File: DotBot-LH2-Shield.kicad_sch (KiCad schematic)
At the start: 15 parts, among them J1 Conn_01x04, J1 Conn_01x10, U1 LSM303AGR, U4 TS4231

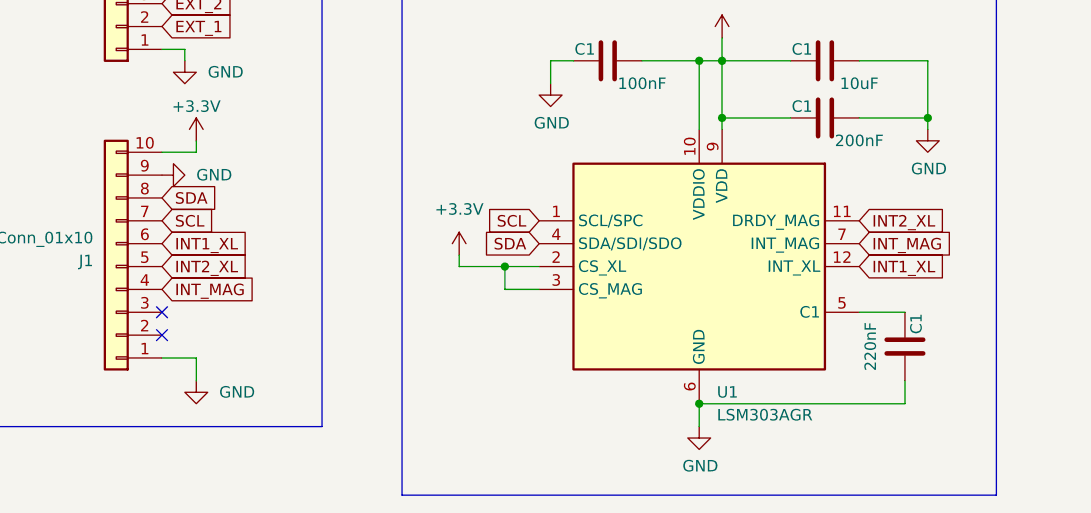
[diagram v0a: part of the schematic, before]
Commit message: Add LH2 shield BOM
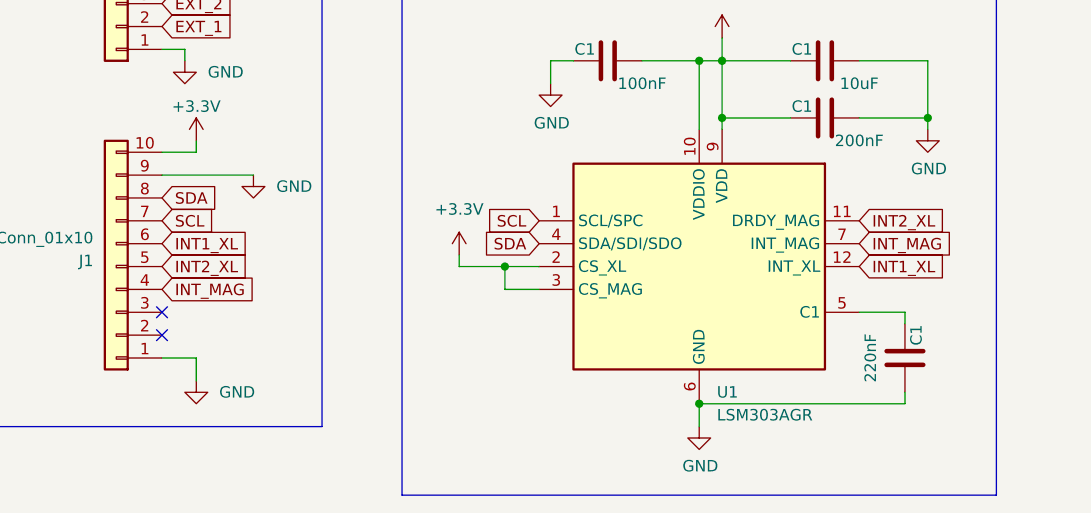
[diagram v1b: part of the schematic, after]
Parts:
- C1, C9: Price $0.005 -> 0.005
- C2: Price $0.0085 -> 0.0085
- D1: Price $0.49 -> 0.49
- D2: Price $0.146 -> 0.146
- J1: Price (none) -> 0.0
- R2: Price $0.0043 -> 0.0043
- U1: Link (none) -> https://www.digikey.fr/short/cm902n73; Mfr Part Number (none) -> 497-16527-1-ND; Price (none) -> 3.026
- U4: Price $0.945 -> 0.945
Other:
- moved on the sheet: C1
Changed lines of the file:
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@@
+    (stroke (width 0) (type default))
+  )
+  (wire (pts (xy 130.81 123.19) (xy 130.81 121.92))
     (stroke (width 0) (type default))
   )
@@
     (stroke (width 0) (type default))
   )
+  (wire (pts (xy 130.81 121.92) (xy 125.73 121.92))
+    (stroke (width 0) (type default))
+  )
   (wire (pts (xy 48.26 45.72) (xy 52.07 45.72))
     (stroke (width 0) (type default))
@@
     (stroke (width 0) (type default))
   )
-  (wire (pts (xy 130.81 129.54) (xy 130.81 132.08))
+  (wire (pts (xy 130.81 130.81) (xy 130.81 132.08))
     (stroke (width 0) (type default))
   )
@@
     (stroke (width 0) (type default))
   )
+  (wire (pts (xy 48.26 106.68) (xy 58.42 106.68))
+    (stroke (width 0) (type default))
+  )
   (wire (pts (xy 97.79 63.5) (xy 101.6 63.5))
     (stroke (width 0) (type default))
@@
   )
   (wire (pts (xy 133.35 93.98) (xy 133.35 100.33))
-    (stroke (width 0) (type default))
-  )
-  (wire (pts (xy 125.73 121.92) (xy 130.81 121.92))
     (stroke (width 0) (type default))
   )
@@
       (effects (font (size 1.27 1.27)) hide)
     )
-    (property "Price" "$0.146" (at 179.07 53.34 0)
+    (property "Price" "0.146" (at 179.07 53.34 0)
       (effects (font (size 1.27 1.27)) hide)
     )
@@
       (effects (font (size 1.27 1.27)) hide)
     )
-    (property "Price" "$0.005" (at 121.92 100.33 0)
+    (property "Price" "0.005" (at 121.92 100.33 0)
       (effects (font (size 1.27 1.27)) hide)
     )
@@
     )
   )
-  (symbol (lib_id "Device:C") (at 130.81 125.73 180) (unit 1)
-    (in_bom yes) (on_board yes) (dnp no)
-    (property "Reference" "C1" (at 132.08 123.19 90)
-      (effects (font (size 1.27 1.27)))
-    )
-    (property "Value" "220nF" (at 127 125.73 90)
-      (effects (font (size 1.27 1.27)))
-    )
-    (property "Footprint" "Capacitor_SMD:C_0603_1608Metric" (at 129.8448 121.92 0)
-      (effects (font (size 1.27 1.27)) hide)
-    )
-    (property "Datasheet" "http://www.samsungsem.com/kr/support/product-search/mlcc/CL10B104KB8NNWC.jsp" (at 130.81 125.73 0)
-      (effects (font (size 1.27 1.27)) hide)
-    )
-    (property "Link" "https://www.digikey.fr/short/pm3hbfq0" (at 130.81 125.73 0)
-      (effects (font (size 1.27 1.27)) hide)
-    )
-    (property "Mfr Part Number" "CL10B104KB8NNWC" (at 130.81 125.73 0)
-      (effects (font (size 1.27 1.27)) hide)
-    )
-    (property "Price" "$0.005" (at 130.81 125.73 0)
+  (symbol (lib_id "Device:C") (at 130.81 127 180) (unit 1)
+    (in_bom yes) (on_board yes) (dnp no)
+    (property "Reference" "C1" (at 132.08 124.46 90)
+      (effects (font (size 1.27 1.27)))
+    )
+    (property "Value" "220nF" (at 127 127 90)
+      (effects (font (size 1.27 1.27)))
+    )
+    (property "Footprint" "Capacitor_SMD:C_0603_1608Metric" (at 129.8448 123.19 0)
+      (effects (font (size 1.27 1.27)) hide)
+    )
+    (property "Datasheet" "http://www.samsungsem.com/kr/support/product-search/mlcc/CL10B104KB8NNWC.jsp" (at 130.81 127 0)
+      (effects (font (size 1.27 1.27)) hide)
+    )
+    (property "Link" "https://www.digikey.fr/short/pm3hbfq0" (at 130.81 127 0)
+      (effects (font (size 1.27 1.27)) hide)
+    )
+    (property "Mfr Part Number" "CL10B104KB8NNWC" (at 130.81 127 0)
+      (effects (font (size 1.27 1.27)) hide)
+    )
+    (property "Price" "0.005" (at 130.81 127 0)
       (effects (font (size 1.27 1.27)) hide)
     )
@@
     )
     (property "Datasheet" "~" (at 43.18 116.84 0)
+      (effects (font (size 1.27 1.27)) hide)
+    )
+    (property "Price" "0.0" (at 43.18 116.84 0)
       (effects (font (size 1.27 1.27)) hide)
     )
@@
     )
   )
-  (symbol (lib_id "OLIMEX_Power:GND") (at 48.26 106.68 90) (unit 1)
+  (symbol (lib_id "OLIMEX_Power:GND") (at 58.42 106.68 0) (unit 1)
     (in_bom yes) (on_board yes) (dnp no) (fields_autoplaced)
-    (property "Reference" "#PWR01" (at 54.61 106.68 0)
-      (effects (font (size 1.27 1.27)) hide)
-    )
-    (property "Value" "GND" (at 52.07 106.68 90)
-      (effects (font (size 1.27 1.27)) (justify right))
-    )
-    (property "Footprint" "" (at 48.26 106.68 0)
-      (effects (font (size 1.524 1.524)))
-    )
-    (property "Datasheet" "" (at 48.26 106.68 0)
+    (property "Reference" "#PWR01" (at 58.42 113.03 0)
+      (effects (font (size 1.27 1.27)) hide)
+    )
+    (property "Value" "GND" (at 60.96 107.95 0)
+      (effects (font (size 1.27 1.27)) (justify left))
+    )
+    (property "Footprint" "" (at 58.42 106.68 0)
+      (effects (font (size 1.524 1.524)))
+    )
+    (property "Datasheet" "" (at 58.42 106.68 0)
       (effects (font (size 1.524 1.524)))
     )
@@
       (effects (font (size 1.27 1.27)) hide)
     )
-    (property "Price" "$0.0043" (at 138.43 55.88 0)
+    (property "Price" "0.0043" (at 138.43 55.88 0)
       (effects (font (size 1.27 1.27)) hide)
     )
@@
       (effects (font (size 1.27 1.27)) hide)
     )
-    (property "Price" "$0.49" (at 90.17 63.5 0)
+    (property "Price" "0.49" (at 90.17 63.5 0)
       (effects (font (size 1.27 1.27)) hide)
     )
@@
       (effects (font (size 1.27 1.27)) hide)
     )
-    (property "Price" "$0.945" (at 120.65 43.18 0)
+    (property "Price" "0.945" (at 120.65 43.18 0)
       (effects (font (size 1.27 1.27)) hide)
     )
@@
       (effects (font (size 1.27 1.27)) hide)
     )
-    (property "Price" "$0.005" (at 97.79 93.98 0)
+    (property "Price" "0.005" (at 97.79 93.98 0)
       (effects (font (size 1.27 1.27)) hide)
     )
@@
       (effects (font (size 1.27 1.27)) hide)
     )
-    (property "Price" "$0.005" (at 121.92 93.98 0)
+    (property "Price" "0.005" (at 121.92 93.98 0)
       (effects (font (size 1.27 1.27)) hide)
     )
@@
       (effects (font (size 1.27 1.27)) hide)
     )
-    (property "Price" "$0.005" (at 186.69 67.31 0)
+    (property "Price" "0.005" (at 186.69 67.31 0)
       (effects (font (size 1.27 1.27)) hide)
     )
@@
     )
     (property "Datasheet" "www.st.com/resource/en/datasheet/lsm303c.pdf" (at 110.49 133.35 0)
+      (effects (font (size 1.27 1.27)) hide)
+    )
+    (property "Link" "https://www.digikey.fr/short/cm902n73" (at 107.95 116.84 0)
+      (effects (font (size 1.27 1.27)) hide)
+    )
+    (property "Mfr Part Number" "497-16527-1-ND" (at 107.95 116.84 0)
+      (effects (font (size 1.27 1.27)) hide)
+    )
+    (property "Price" "3.026" (at 107.95 116.84 0)
       (effects (font (size 1.27 1.27)) hide)
     )
@@
       (effects (font (size 1.27 1.27)) hide)
     )
-    (property "Price" "$0.0085" (at 90.17 54.61 0)
+    (property "Price" "0.0085" (at 90.17 54.61 0)
       (effects (font (size 1.27 1.27)) hide)
     )
@@
     )
     (property "Datasheet" "~" (at 43.18 50.8 0)
+      (effects (font (size 1.27 1.27)) hide)
+    )
+    (property "Price" "0.0" (at 43.18 50.8 0)
       (effects (font (size 1.27 1.27)) hide)
     )
@@
     )
     (property "Datasheet" "~" (at 43.18 82.55 0)
+      (effects (font (size 1.27 1.27)) hide)
+    )
+    (property "Price" "0.0" (at 43.18 82.55 0)
       (effects (font (size 1.27 1.27)) hide)
     )
@@
       (effects (font (size 1.27 1.27)) hide)
     )
-    (property "Price" "$0.005" (at 90.17 48.26 0)
-      (effects (font (size 1.27 1.27)) hide)
-    )
+    (property "Price" "0.005" (at 90.17 48.26 0)
+      (effects (font (size 1.27 1.27)) hide)
+    )

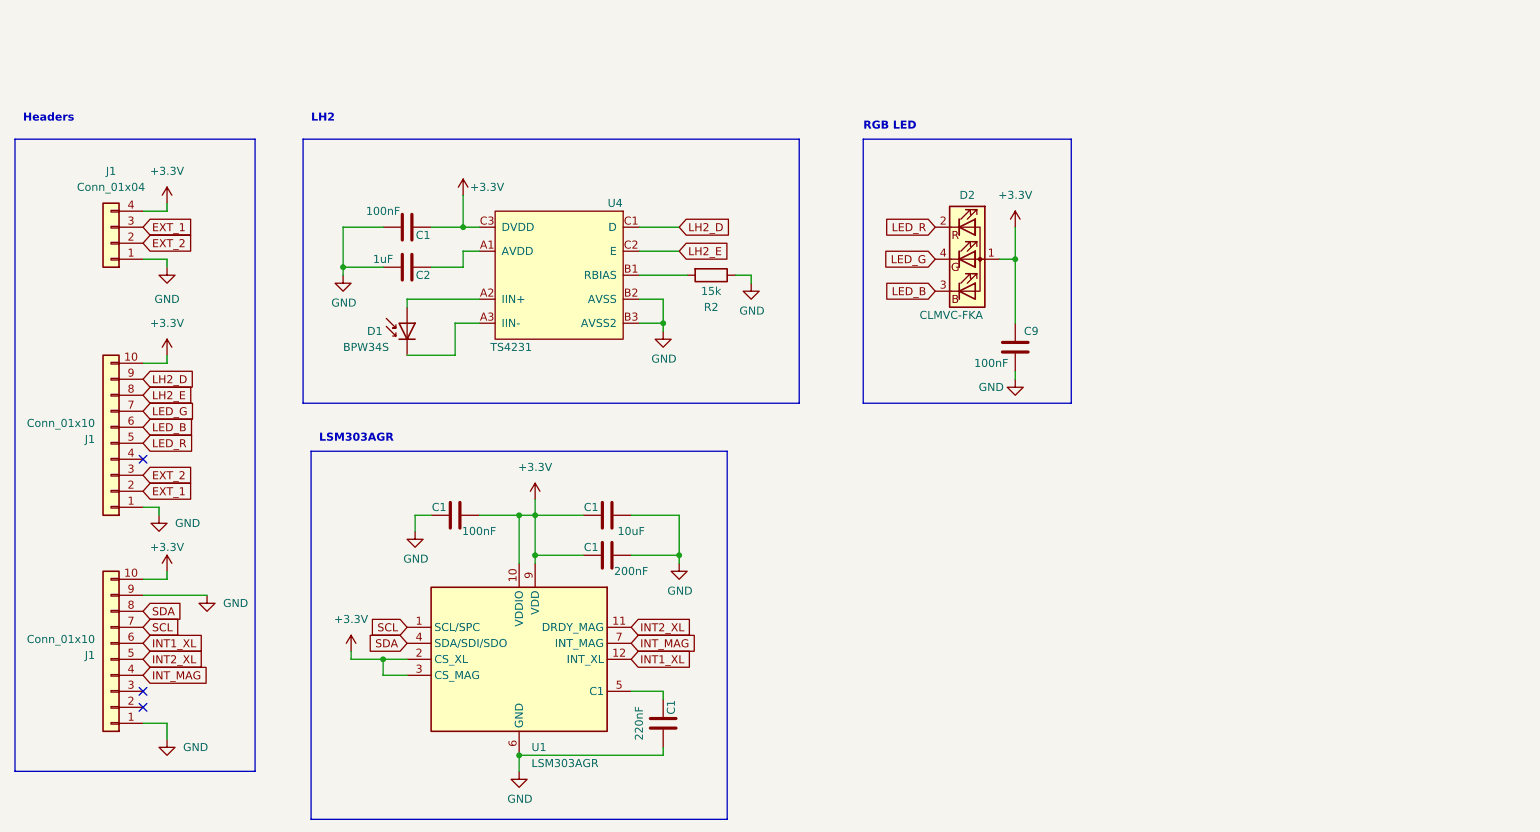
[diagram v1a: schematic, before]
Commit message: DotBot-LH2-Shield: expose 6V and use it for RGB LED. rework IMU layout abit
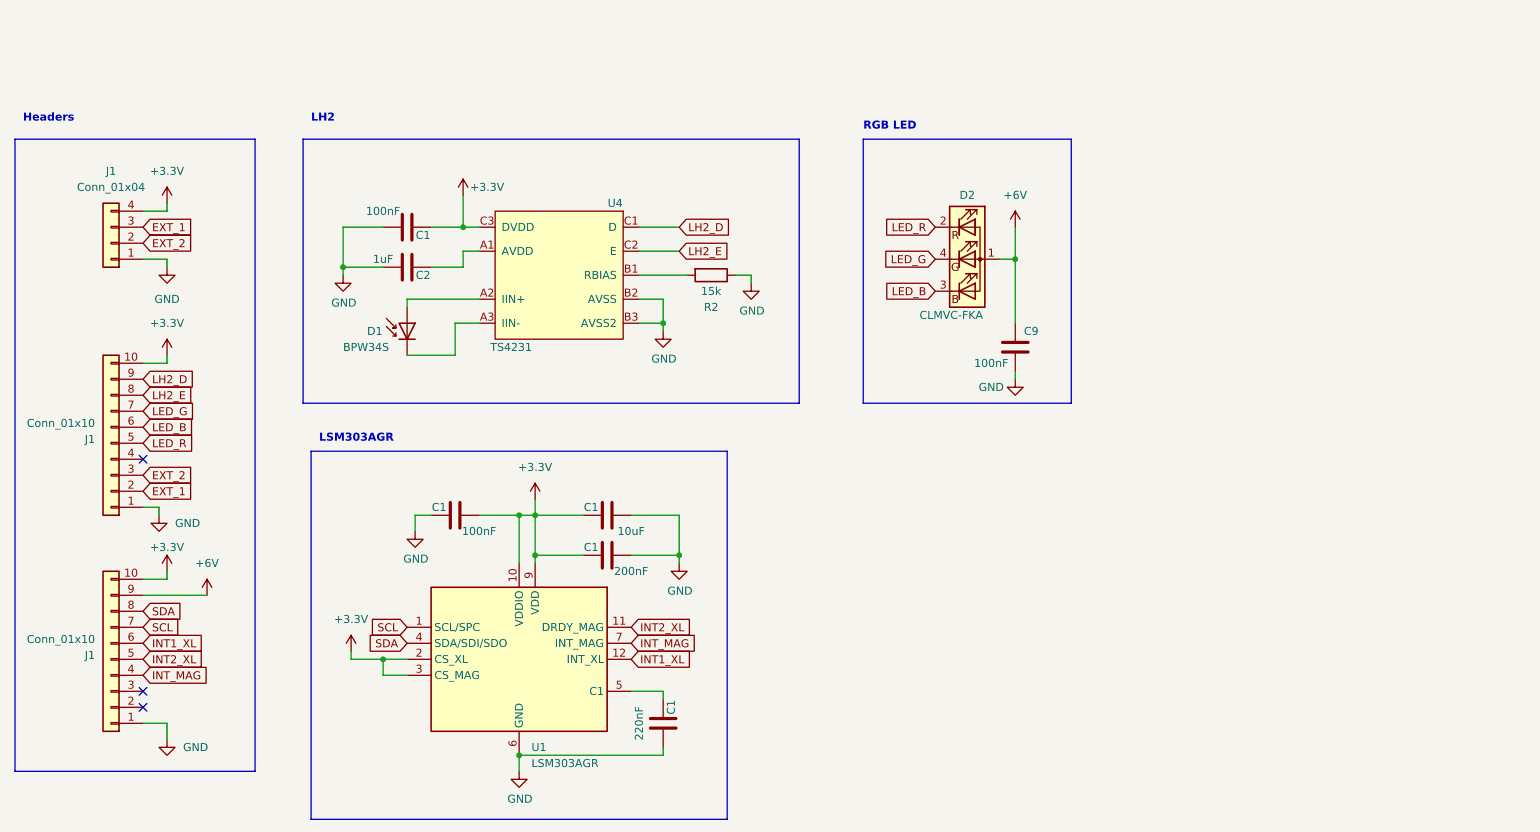
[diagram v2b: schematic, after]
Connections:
- net +3V3: no longer C9.1, D2.1 (A)
- net GND: no longer J1.9 (Pin_9)
- new net +6V: C9.1, D2.1 (A), J1.9 (Pin_9)
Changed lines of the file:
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@@
+    )
+  )
+  (symbol (lib_id "OLIMEX_Power:+6V") (at 186.69 48.26 0) (unit 1)
+    (in_bom yes) (on_board yes) (dnp no) (fields_autoplaced)
+    (property "Reference" "#PWR017" (at 186.69 52.07 0)
+      (effects (font (size 1.27 1.27)) hide)
+    )
+    (property "Value" "+6V" (at 186.69 43.18 0)
+      (effects (font (size 1.27 1.27)))
+    )
+    (property "Footprint" "" (at 186.69 48.26 0)
+      (effects (font (size 1.524 1.524)))
+    )
+    (property "Datasheet" "" (at 186.69 48.26 0)
+      (effects (font (size 1.524 1.524)))
+    )
+    (pin "1")
+    (instances
+      (project "DotBot-LH2-Shield"
+        (path "/92e40173-df06-4aa6-9ab0-efc512328572"
+          (reference "#PWR017") (unit 1)
+        )
+      )
     )
   )
@@
     )
   )
-  (symbol (lib_id "OLIMEX_Power:GND") (at 58.42 106.68 0) (unit 1)
-    (in_bom yes) (on_board yes) (dnp no) (fields_autoplaced)
-    (property "Reference" "#PWR01" (at 58.42 113.03 0)
-      (effects (font (size 1.27 1.27)) hide)
-    )
-    (property "Value" "GND" (at 60.96 107.95 0)
-      (effects (font (size 1.27 1.27)) (justify left))
-    )
-    (property "Footprint" "" (at 58.42 106.68 0)
-      (effects (font (size 1.524 1.524)))
-    )
-    (property "Datasheet" "" (at 58.42 106.68 0)
-      (effects (font (size 1.524 1.524)))
-    )
-    (pin "1")
-    (instances
-      (project "DotBot-LH2-Shield"
-        (path "/92e40173-df06-4aa6-9ab0-efc512328572"
-          (reference "#PWR01") (unit 1)
-        )
-      )
-    )
-  )
   (symbol (lib_id "OLIMEX_Power:+3.3V") (at 52.07 102.87 0) (unit 1)
     (in_bom yes) (on_board yes) (dnp no)
@@
         (path "/92e40173-df06-4aa6-9ab0-efc512328572"
           (reference "D1") (unit 1)
-        )
-      )
-    )
-  )
-  (symbol (lib_id "OLIMEX_Power:+3.3V") (at 186.69 48.26 0) (unit 1)
-    (in_bom yes) (on_board yes) (dnp no) (fields_autoplaced)
-    (property "Reference" "#PWR017" (at 186.69 52.07 0)
-      (effects (font (size 1.27 1.27)) hide)
-    )
-    (property "Value" "+3.3V" (at 186.69 43.18 0)
-      (effects (font (size 1.27 1.27)))
-    )
-    (property "Footprint" "" (at 186.69 48.26 0)
-      (effects (font (size 1.524 1.524)))
-    )
-    (property "Datasheet" "" (at 186.69 48.26 0)
-      (effects (font (size 1.524 1.524)))
-    )
-    (pin "1")
-    (instances
-      (project "DotBot-LH2-Shield"
-        (path "/92e40173-df06-4aa6-9ab0-efc512328572"
-          (reference "#PWR017") (unit 1)
         )
       )
@@
         )
       )
+    )
+  )
+  (symbol (lib_id "OLIMEX_Power:+6V") (at 58.42 106.68 0) (unit 1)
+    (in_bom yes) (on_board yes) (dnp no) (fields_autoplaced)
+    (property "Reference" "#PWR01" (at 58.42 110.49 0)
+      (effects (font (size 1.27 1.27)) hide)
+    )
+    (property "Value" "+6V" (at 58.42 101.6 0)
+      (effects (font (size 1.27 1.27)))
+    )
+    (property "Footprint" "" (at 58.42 106.68 0)
+      (effects (font (size 1.524 1.524)))
+    )
+    (property "Datasheet" "" (at 58.42 106.68 0)
+      (effects (font (size 1.524 1.524)))
+    )
+    (pin "1")
+    (instances
+      (project "DotBot-LH2-Shield"
+        (path "/92e40173-df06-4aa6-9ab0-efc512328572"
+          (reference "#PWR01") (unit 1)
+        )
+      )
